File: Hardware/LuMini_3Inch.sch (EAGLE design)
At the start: 69 parts, among them J1 DOUBLE_LED_PAD, J2 DOUBLE_LED_PAD, J3 DOUBLE_LED_PAD

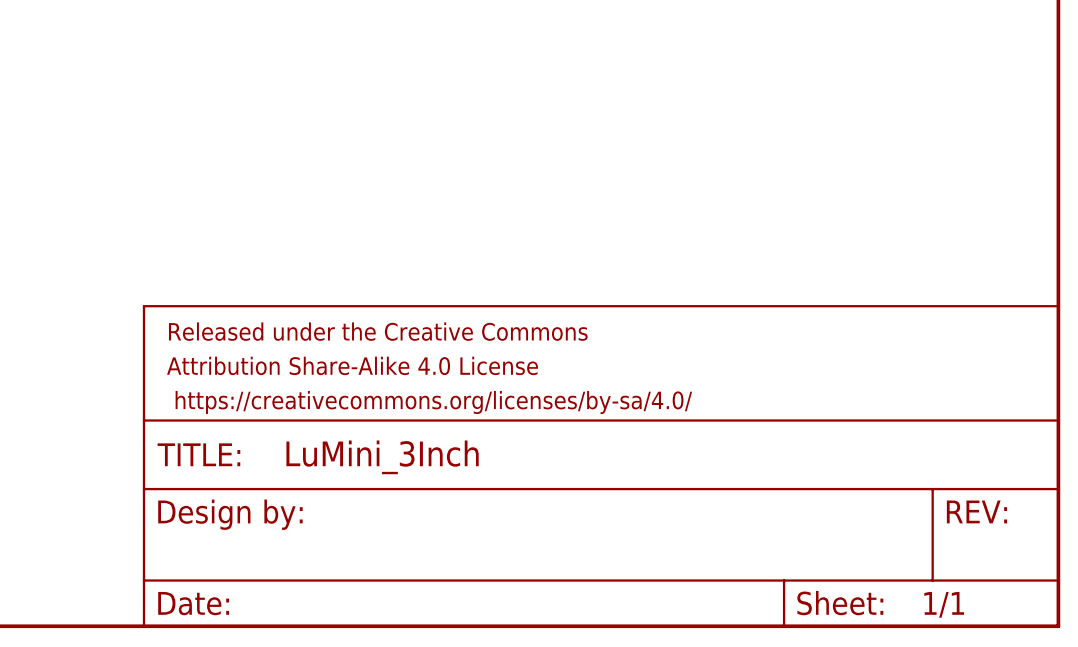
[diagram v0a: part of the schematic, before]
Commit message: adding silk
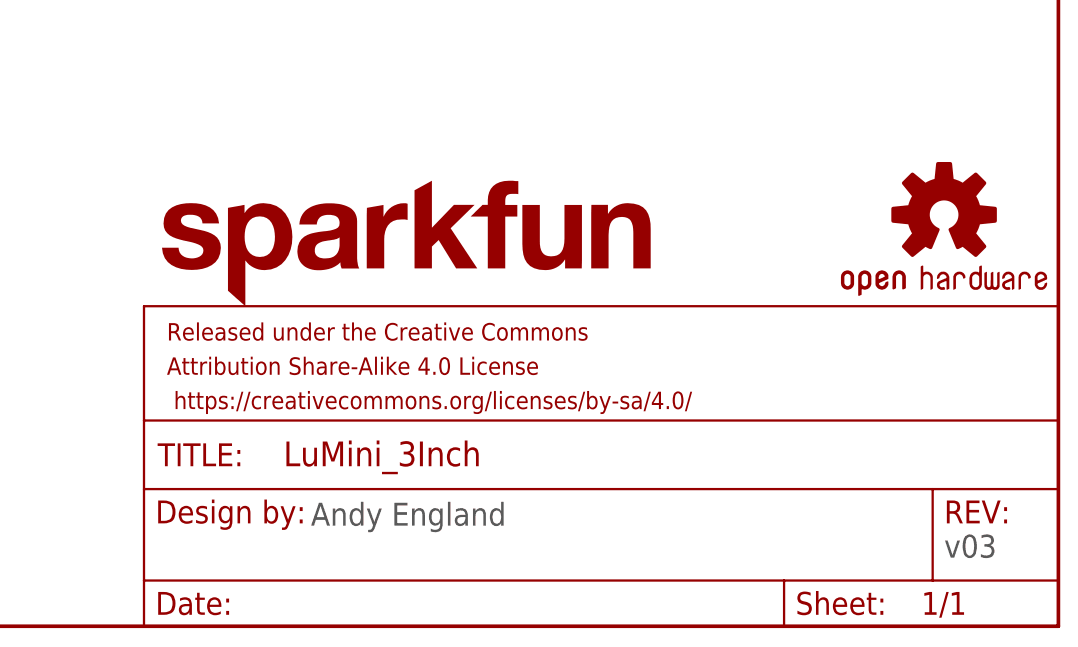
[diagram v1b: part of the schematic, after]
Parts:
- added LOGO1: OSHW-LOGOS, SparkFun-Aesthetics:OSHW-LOGOS
- added LOGO2: SFE_LOGO_NAME.1_INCH, SparkFun-Aesthetics:SFE_LOGO_NAME.1_INCH
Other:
- note added: "Andy England"
- note added: "v03"
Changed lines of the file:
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@@
 <part name="GND62" library="SparkFun-PowerSymbols" deviceset="GND" device=""/>
 <part name="SUPPLY17" library="SparkFun-PowerSymbols" deviceset="5V" device=""/>
+<part name="LOGO1" library="SparkFun-Aesthetics" deviceset="OSHW-LOGO" device="S"/>
+<part name="LOGO2" library="SparkFun-Aesthetics" deviceset="SFE_LOGO_NAME" device=".1_INCH"/>
 </parts>
 <sheets>
@@
 <text x="180.34" y="124.46" size="3.81" layer="94" font="vector">Grounding Standoffs</text>
 <wire x1="0" y1="144.78" x2="431.8" y2="144.78" width="0.2032" layer="97" style="longdash"/>
+<text x="348.742" y="11.176" size="2.54" layer="97" font="vector">Andy England</text>
+<text x="419.1" y="7.62" size="2.54" layer="97" font="vector">v03</text>
 </plain>
 <instances>
@@
 <instance part="GND62" gate="1" x="281.94" y="83.82"/>
 <instance part="SUPPLY17" gate="G$1" x="281.94" y="99.06"/>
+<instance part="LOGO1" gate="G$1" x="419.1" y="45.72"/>
+<instance part="LOGO2" gate="G$1" x="330.2" y="35.56"/>
 </instances>
 <busses>

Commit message: post checklist
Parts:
- added FD1, FD2, FD3, FD4: FIDUCIALUFIDUCIAL, SparkFun-Aesthetics:FIDUCIALUFIDUCIAL
- added H5, H6, H7, H8: STANDOFF_ELECTRICALSTANDOFF-ELECTRICAL-NOTHERMALS, SparkFun-Hardware:STANDOFF_ELECTRICALSTANDOFF-ELECTRICAL-NOTHERMALS
- C1: value 4.7uF -> DNP; device SparkFun-Capacitors:4.7UF-0603-6.3V-(10%) -> SparkFun-Capacitors:4.7UF-1206-16V-(+80/-20%)
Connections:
- net GND: now also H5.P$1, H6.P$1, H7.P$1, H8.P$1
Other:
- note added: "Vin: 3.0V-5.5V"
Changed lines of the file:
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@@
 <part name="H4" library="SparkFun-Hardware" deviceset="STANDOFF_ELECTRICAL" device="STANDOFF-ELECTRICAL-NOTHERMALS" value="STANDOFF_ELECTRICALSTANDOFF-ELECTRICAL-NOTHERMALS"/>
 <part name="GND17" library="SparkFun-PowerSymbols" deviceset="GND" device=""/>
-<part name="C1" library="SparkFun-Capacitors" deviceset="4.7UF" device="-0603-6.3V-(10%)" value="4.7uF"/>
+<part name="C1" library="SparkFun-Capacitors" deviceset="4.7UF" device="-1206-16V-(+80/-20%)" value="DNP"/>
 <part name="GND62" library="SparkFun-PowerSymbols" deviceset="GND" device=""/>
 <part name="SUPPLY17" library="SparkFun-PowerSymbols" deviceset="5V" device=""/>
 <part name="LOGO1" library="SparkFun-Aesthetics" deviceset="OSHW-LOGO" device="S"/>
 <part name="LOGO2" library="SparkFun-Aesthetics" deviceset="SFE_LOGO_NAME" device=".1_INCH"/>
+<part name="H5" library="SparkFun-Hardware" deviceset="STANDOFF_ELECTRICAL" device="STANDOFF-ELECTRICAL-NOTHERMALS" value="STANDOFF_ELECTRICALSTANDOFF-ELECTRICAL-NOTHERMALS"/>
+<part name="H6" library="SparkFun-Hardware" deviceset="STANDOFF_ELECTRICAL" device="STANDOFF-ELECTRICAL-NOTHERMALS" value="STANDOFF_ELECTRICALSTANDOFF-ELECTRICAL-NOTHERMALS"/>
+<part name="H7" library="SparkFun-Hardware" deviceset="STANDOFF_ELECTRICAL" device="STANDOFF-ELECTRICAL-NOTHERMALS" value="STANDOFF_ELECTRICALSTANDOFF-ELECTRICAL-NOTHERMALS"/>
+<part name="H8" library="SparkFun-Hardware" deviceset="STANDOFF_ELECTRICAL" device="STANDOFF-ELECTRICAL-NOTHERMALS" value="STANDOFF_ELECTRICALSTANDOFF-ELECTRICAL-NOTHERMALS"/>
+<part name="FD1" library="SparkFun-Aesthetics" deviceset="FIDUCIAL" device="UFIDUCIAL"/>
+<part name="FD2" library="SparkFun-Aesthetics" deviceset="FIDUCIAL" device="UFIDUCIAL"/>
+<part name="FD3" library="SparkFun-Aesthetics" deviceset="FIDUCIAL" device="UFIDUCIAL"/>
+<part name="FD4" library="SparkFun-Aesthetics" deviceset="FIDUCIAL" device="UFIDUCIAL"/>
 </parts>
 <sheets>
 <sheet>
 <plain>
-<text x="200.66" y="264.16" size="3.81" layer="94" font="vector">LED's</text>
-<text x="180.34" y="124.46" size="3.81" layer="94" font="vector">Grounding Standoffs</text>
+<text x="200.66" y="264.16" size="3.81" layer="97" font="vector">LED's</text>
+<text x="180.34" y="124.46" size="3.81" layer="97" font="vector">Grounding Standoffs</text>
 <wire x1="0" y1="144.78" x2="431.8" y2="144.78" width="0.2032" layer="97" style="longdash"/>
 <text x="348.742" y="11.176" size="2.54" layer="97" font="vector">Andy England</text>
 <text x="419.1" y="7.62" size="2.54" layer="97" font="vector">v03</text>
+<text x="200.66" y="261.62" size="1.778" layer="97" font="vector">Vin: 3.0V-5.5V</text>
 </plain>
 <instances>
@@
 <instance part="H3" gate="G$1" x="203.2" y="81.28" rot="R180"/>
 <instance part="H4" gate="G$1" x="203.2" y="66.04" rot="R180"/>
-<instance part="GND17" gate="1" x="193.04" y="60.96"/>
+<instance part="GND17" gate="1" x="193.04" y="53.34"/>
 <instance part="C1" gate="G$1" x="281.94" y="91.44"/>
 <instance part="GND62" gate="1" x="281.94" y="83.82"/>
@@
 <instance part="LOGO1" gate="G$1" x="419.1" y="45.72"/>
 <instance part="LOGO2" gate="G$1" x="330.2" y="35.56"/>
+<instance part="H5" gate="G$1" x="182.88" y="111.76"/>
+<instance part="H6" gate="G$1" x="182.88" y="93.98"/>
+<instance part="H7" gate="G$1" x="182.88" y="78.74"/>
+<instance part="H8" gate="G$1" x="182.88" y="63.5"/>
+<instance part="FD1" gate="G$1" x="414.02" y="20.32"/>
+<instance part="FD2" gate="G$1" x="416.56" y="20.32"/>
+<instance part="FD3" gate="G$1" x="419.1" y="20.32"/>
+<instance part="FD4" gate="G$1" x="421.64" y="20.32"/>
 </instances>
 <busses>
@@
 <wire x1="193.04" y1="111.76" x2="193.04" y2="96.52" width="0.1524" layer="91"/>
 <pinref part="H4" gate="G$1" pin="P$1"/>
-<wire x1="193.04" y1="96.52" x2="193.04" y2="81.28" width="0.1524" layer="91"/>
-<wire x1="193.04" y1="81.28" x2="193.04" y2="66.04" width="0.1524" layer="91"/>
+<wire x1="193.04" y1="96.52" x2="193.04" y2="93.98" width="0.1524" layer="91"/>
+<wire x1="193.04" y1="93.98" x2="193.04" y2="81.28" width="0.1524" layer="91"/>
+<wire x1="193.04" y1="81.28" x2="193.04" y2="78.74" width="0.1524" layer="91"/>
+<wire x1="193.04" y1="78.74" x2="193.04" y2="66.04" width="0.1524" layer="91"/>
 <wire x1="193.04" y1="66.04" x2="193.04" y2="63.5" width="0.1524" layer="91"/>
+<wire x1="193.04" y1="63.5" x2="193.04" y2="55.88" width="0.1524" layer="91"/>
 <wire x1="195.58" y1="66.04" x2="193.04" y2="66.04" width="0.1524" layer="91"/>
 <junction x="193.04" y="66.04"/>
@@
 <wire x1="195.58" y1="96.52" x2="193.04" y2="96.52" width="0.1524" layer="91"/>
 <junction x="193.04" y="96.52"/>
-</segment>
-<segment>
+<pinref part="H5" gate="G$1" pin="P$1"/>
+<wire x1="193.04" y1="111.76" x2="190.5" y2="111.76" width="0.1524" layer="91"/>
+<junction x="193.04" y="111.76"/>
+<pinref part="H6" gate="G$1" pin="P$1"/>
+<wire x1="190.5" y1="93.98" x2="193.04" y2="93.98" width="0.1524" layer="91"/>
+<junction x="193.04" y="93.98"/>
+<pinref part="H7" gate="G$1" pin="P$1"/>
+<wire x1="193.04" y1="78.74" x2="190.5" y2="78.74" width="0.1524" layer="91"/>
+<junction x="193.04" y="78.74"/>
+<pinref part="H8" gate="G$1" pin="P$1"/>
+<wire x1="190.5" y1="63.5" x2="193.04" y2="63.5" width="0.1524" layer="91"/>
+<junction x="193.04" y="63.5"/>
+</segment>
+<segment>

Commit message: cleaning up schematic
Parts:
- H1, H2, H3, H4, H5, H6, H7, H8: value STANDOFF_ELECTRICALSTANDOFF-ELECTRICAL-NOTHERMALS -> STANDOFF_ELECTRICAL-NOTHERMALS; device SparkFun-Hardware:STANDOFF_ELECTRICALSTANDOFF-ELECTRICAL-NOTHERMALS -> SparkFun-Hardware:STANDOFF_ELECTRICAL-NOTHERMALS
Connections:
- net N$122 renamed CO
- net N$123 renamed DO
- net N$2 renamed CI
- net N$3 renamed DI
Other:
- note added: "Optional Decoupling Capacitor"
- note added: "Solder Pads"
- moved on the sheet: C1, H1, H2, H3, H4, H5, H6, H7, H8, J1, J2, J3
